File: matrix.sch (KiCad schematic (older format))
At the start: 138 parts, among them SW1 Esc, SW10 #9, SW11 #0, SW12 -_, SW13 BSPC, SW14 Delete, SW15 Home, SW16 TAB, SW17 Q, SW18 W, SW19 E, SW2 #1, SW20 R, SW21 T, SW22 Y, SW23 U, SW24 I, SW25 O, SW26 P, SW27 [{, SW28 ]}, SW29 \\|, SW3 #2, SW30 END, SW31 CAPS, SW32 A, SW33 S, SW34 D, SW35 F, SW36 G, SW37 H, SW38 J, SW39 K, SW4 #3, SW40 L, SW41 ;:, SW42 '\", SW43 ENTR, SW44 PGUP, SW45 LSFT, SW46 Z, SW47 X, SW48 C, SW49 V, SW5 #4, SW50 B, SW51 N, SW52 M, SW53 ,<, SW54 .>, SW55 /?, SW56 =+, SW57 RSFT, SW58 UP, SW59 PGDN, SW6 #5, SW60 LCTL, SW61 LWIN, SW62 LALT, SW63 SPACE, SW64 SPACE, SW65 SPACE, SW66 FN, SW67 LEFT, SW68 DOWN, SW69 RIGHT, SW7 #6, SW8 #7, SW9 #8

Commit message: wired differential
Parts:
- added SW71: BSPC, MX_Only:MXOnly-2U-Hotswap-ReversedStabilizers, symbol Switch:SW_Push
- added SW72: CAPS, MX_Only:MXOnly-1.75U-Hotswap, symbol Switch:SW_Push
- D1, D10, D11, D12, D13, D14, D15, D16, D17, D18, D19, D2, D20, D21, D22, D23, D24, D25, D26, D27, D28, D29, D3, D30, D31, D32, D33, D34, D35, D36, D37, D38, D39, D4, D40, D41, D42, D43, D44, D45, D46, D47, D48, D49, D5, D50, D51, D52, D53, D54, D55, D56, D57, D58, D59, D6, D60, D61, D62, D63, D64, D65, D66, D67, D68, D69, D7, D8, D9: footprint (none) -> Diode_SMD:D_SOD-123
- SW1, SW10, SW11, SW12, SW13, SW14, SW15, SW17, SW18, SW19, SW2, SW20, SW21, SW22, SW23, SW24, SW25, SW26, SW27, SW28, SW3, SW30, SW31, SW32, SW33, SW34, SW35, SW36, SW37, SW38, SW39, SW4, SW40, SW41, SW42, SW44, SW46, SW47, SW48, SW49, SW5, SW50, SW51, SW52, SW53, SW54, SW55, SW56, SW58, SW59, SW6, SW61, SW67, SW68, SW69, SW7, SW8, SW9: footprint (none) -> MX_Only:MXOnly-1U-Hotswap
- SW16, SW29, SW60, SW62, SW66: footprint (none) -> MX_Only:MXOnly-1.5U-Hotswap
- SW43, SW45: footprint (none) -> MX_Only:MXOnly-2.25U-Hotswap
- SW57: footprint (none) -> MX_Only:MXOnly-1.75U-Hotswap
- SW63, SW65: footprint (none) -> MX_Only:MXOnly-3U-Hotswap-ReversedStabilizers
- SW64: footprint (none) -> MX_Only:MXOnly-7U-Hotswap-ReversedStabilizers
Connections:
- net col0: now also SW16.2, SW31.2, SW45.2, SW60.2, SW72.2
- net col1: now also SW17.2, SW32.2, SW46.2, SW61.2
- net col10: now also SW26.2, SW41.2, SW55.2
- net col11: now also SW27.2, SW42.2, SW56.2
- net col12: now also SW28.2, SW43.2, SW57.2, SW67.2, SW71.2
- net col13: now also SW29.2, SW58.2, SW68.2
- net col2: now also SW18.2, SW33.2, SW47.2, SW62.2
- net col3: now also SW19.2, SW34.2, SW48.2, SW63.2
- net col4: now also SW20.2, SW35.2, SW49.2
- net col5: now also SW21.2, SW36.2, SW50.2, SW64.2
- net col6: now also SW22.2, SW37.2, SW51.2
- net col7: now also SW23.2, SW38.2, SW52.2, SW65.2
- net col8: now also SW24.2, SW39.2, SW53.2
- net col9: now also SW25.2, SW40.2, SW54.2, SW66.2
- net row0: no longer SW16.2, SW17.2, SW18.2, SW19.2, SW20.2, SW21.2, SW22.2, SW23.2, SW24.2, SW25.2, SW26.2, SW27.2, SW28.2, SW29.2
- net row1: no longer SW31.2, SW32.2, SW33.2, SW34.2, SW35.2, SW36.2, SW37.2, SW38.2, SW39.2, SW40.2, SW41.2, SW42.2, SW43.2
- net row2: no longer SW45.2, SW46.2, SW47.2, SW48.2, SW49.2, SW50.2, SW51.2, SW52.2, SW53.2, SW54.2, SW55.2, SW56.2, SW57.2, SW58.2
- net row3: no longer SW60.2, SW61.2, SW62.2, SW63.2, SW64.2, SW65.2, SW66.2, SW67.2, SW68.2
- net at D13.2 (A), SW13.1: now also SW71.1
- net at D31.2 (A), SW31.1: now also SW72.1

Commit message: wiring done?
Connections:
- net col10: now also SW66.2
- net col9: no longer SW66.2
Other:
- moved on the sheet: D66, SW66
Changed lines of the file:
@@
 L Switch:SW_Push SW66
 U 1 1 614E27A0
-P 6950 5200
-F 0 "SW66" H 6950 5485 50  0000 C CNN
-F 1 "FN" H 6950 5394 50  0000 C CNN
-F 2 "MX_Only:MXOnly-1.5U-Hotswap" H 6950 5400 50  0001 C CNN
-F 3 "~" H 6950 5400 50  0001 C CNN
-	1    6950 5200
+P 7600 5200
+F 0 "SW66" H 7600 5485 50  0000 C CNN
+F 1 "FN" H 7600 5394 50  0000 C CNN
+F 2 "MX_Only:MXOnly-1.5U-Hotswap" H 7600 5400 50  0001 C CNN
+F 3 "~" H 7600 5400 50  0001 C CNN
+	1    7600 5200
 	1    0    0    -1
 $EndComp
@@
 L Device:D D66
 U 1 1 614E27AA
-P 6750 5350
-F 0 "D66" V 6796 5270 50  0000 R CNN
-F 1 "D" V 6705 5270 50  0000 R CNN
-F 2 "Diode_SMD:D_SOD-123" H 6750 5350 50  0001 C CNN
-F 3 "~" H 6750 5350 50  0001 C CNN
-	1    6750 5350
+P 7400 5350
+F 0 "D66" V 7446 5270 50  0000 R CNN
+F 1 "D" V 7355 5270 50  0000 R CNN
+F 2 "Diode_SMD:D_SOD-123" H 7400 5350 50  0001 C CNN
+F 3 "~" H 7400 5350 50  0001 C CNN
+	1    7400 5350
 	0    -1   -1   0
 $EndComp
-Connection ~ 6750 5500
 $Comp
 L Switch:SW_Push SW67
@@
 	4800 4700 5450 4700
 Wire Wire Line
-	5450 5500 6750 5500
-Wire Wire Line
 	6100 4700 6750 4700
 Wire Wire Line
 	7400 4700 8050 4700
-Wire Wire Line
-	6750 5500 8700 5500
 Wire Wire Line
 	8050 4700 8700 4700
@@
 Connection ~ 7150 3600
 Wire Wire Line
-	7150 4400 7150 5200
-Connection ~ 7150 4400
+	7800 4400 7800 5200
 Wire Wire Line
 	7800 2000 7800 2800
@@
 	9750 4400 9750 5200
 Connection ~ 9750 4400
+Connection ~ 7400 5500
+Wire Wire Line
+	7400 5500 8700 5500
+Connection ~ 7800 4400
+Wire Wire Line
+	5450 5500 7400 5500
 $EndSCHEMATC

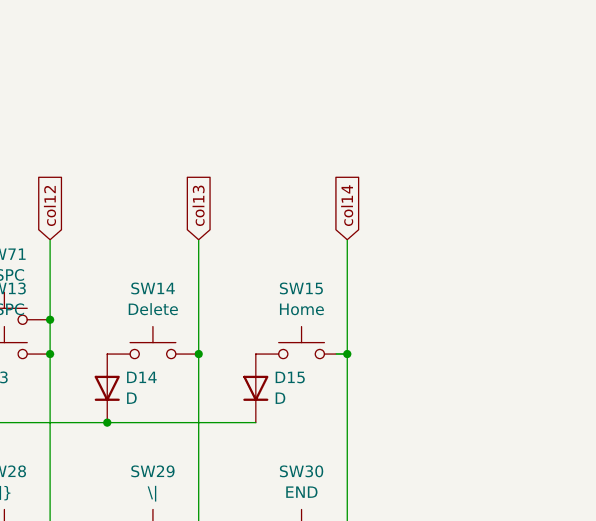
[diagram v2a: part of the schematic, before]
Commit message: added ec11
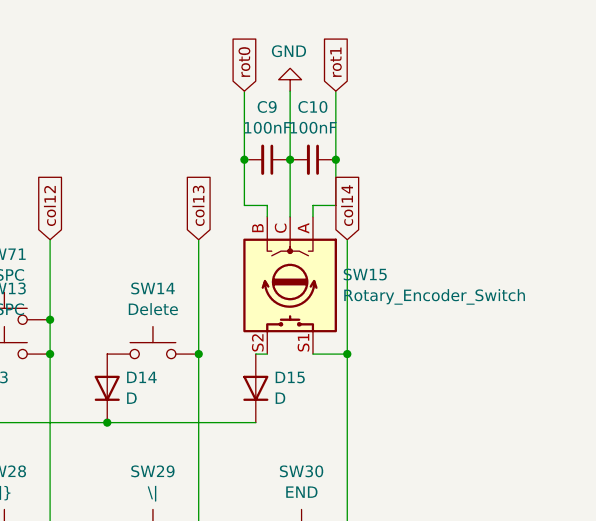
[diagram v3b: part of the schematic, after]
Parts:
- removed SW15: Home, MX_Only:MXOnly-1U-Hotswap, symbol Switch:SW_Push
- added C10, C9: 100nF, Capacitor_SMD:C_0805_2012Metric_Pad1.18x1.45mm_HandSolder, symbol Device:C_Small
- added SW15: Rotary_Encoder_Switch, Keebio-Parts:RotaryEncoder_Alps_EC11E-Switch_Vertical_H20mm, symbol Device:Rotary_Encoder_Switch
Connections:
- net col14: now also SW15.S1
- net at D15.2 (A): now also SW15.S2
- new net GND: C10.2, C9.1, SW15.C
- new net rot0: C9.2, SW15.B
- new net rot1: C10.1, SW15.A
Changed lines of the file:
@@
 Connection ~ 9350 2300
-$Comp
-L Switch:SW_Push SW15
-U 1 1 6141F9AA
-P 10200 2000
-F 0 "SW15" H 10200 2285 50  0000 C CNN
-F 1 "Home" H 10200 2194 50  0000 C CNN
-F 2 "MX_Only:MXOnly-1U-Hotswap" H 10200 2200 50  0001 C CNN
-F 3 "~" H 10200 2200 50  0001 C CNN
-	1    10200 2000
-	1    0    0    -1
-$EndComp
 $Comp
 L Device:D D15
@@
 Wire Wire Line
 	9350 3100 10000 3100
-Wire Wire Line
-	10350 2000 10400 2000
 Connection ~ 10400 2000
 Wire Wire Line
@@
 Wire Wire Line
 	5450 5500 7400 5500
+$Comp
+L Device:Rotary_Encoder_Switch SW15
+U 1 1 613E0EE8
+P 10150 1700
+F 0 "SW15" V 10104 1930 50  0000 L CNN
+F 1 "Rotary_Encoder_Switch" V 10195 1930 50  0000 L CNN
+F 2 "Keebio-Parts:RotaryEncoder_Alps_EC11E-Switch_Vertical_H20mm" H 10000 1860 50  0001 C CNN
+F 3 "~" H 10150 1960 50  0001 C CNN
+	1    10150 1700
+	0    1    1    0
+$EndComp
+Wire Wire Line
+	10250 2000 10400 2000
+Wire Wire Line
+	10000 2000 10050 2000
+$Comp
+L Device:C_Small C9
+U 1 1 61403A0D
+P 10050 1150
+F 0 "C9" V 9821 1150 50  0000 C CNN
+F 1 "100nF" V 9912 1150 50  0000 C CNN
+F 2 "Capacitor_SMD:C_0805_2012Metric_Pad1.18x1.45mm_HandSolder" H 10050 1150 50  0001 C CNN
+F 3 "~" H 10050 1150 50  0001 C CNN
+	1    10050 1150
+	0    1    1    0
+$EndComp
+$Comp
+L Device:C_Small C10
+U 1 1 61404A73
+P 10250 1150
+F 0 "C10" V 10021 1150 50  0000 C CNN
+F 1 "100nF" V 10112 1150 50  0000 C CNN
+F 2 "Capacitor_SMD:C_0805_2012Metric_Pad1.18x1.45mm_HandSolder" H 10250 1150 50  0001 C CNN
+F 3 "~" H 10250 1150 50  0001 C CNN
+	1    10250 1150
+	0    1    1    0
+$EndComp
+Wire Wire Line
+	10050 1400 10050 1350
+Wire Wire Line
+	10050 1350 9950 1350
+Wire Wire Line
+	9950 1350 9950 1150
+Wire Wire Line
+	9950 850  9950 1150
+Connection ~ 9950 1150
+Wire Wire Line
+	10150 1400 10150 1150
+Connection ~ 10150 1150
+Wire Wire Line
+	10150 1150 10150 850
+Wire Wire Line
+	10250 1400 10250 1350
+Wire Wire Line
+	10250 1350 10350 1350
+Wire Wire Line
+	10350 1350 10350 1150
+Wire Wire Line
+	10350 1150 10350 850
+Connection ~ 10350 1150
+Text GLabel 9950 850  1    50   Input ~ 0
+rot0
+Text GLabel 10350 850  1    50   Input ~ 0
+rot1
+$Comp
+L power:GND #PWR0117
+U 1 1 6142B7D1
+P 10150 850
+F 0 "#PWR0117" H 10150 600 50  0001 C CNN
+F 1 "GND" H 10155 677 50  0000 C CNN
+F 2 "" H 10150 850 50  0001 C CNN
+F 3 "" H 10150 850 50  0001 C CNN
+	1    10150 850
+	-1   0    0    1
+$EndComp
 $EndSCHEMATC
